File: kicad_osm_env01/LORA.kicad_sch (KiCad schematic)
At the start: 16 parts, among them J9 Conn_01x06, U16 RAK3172

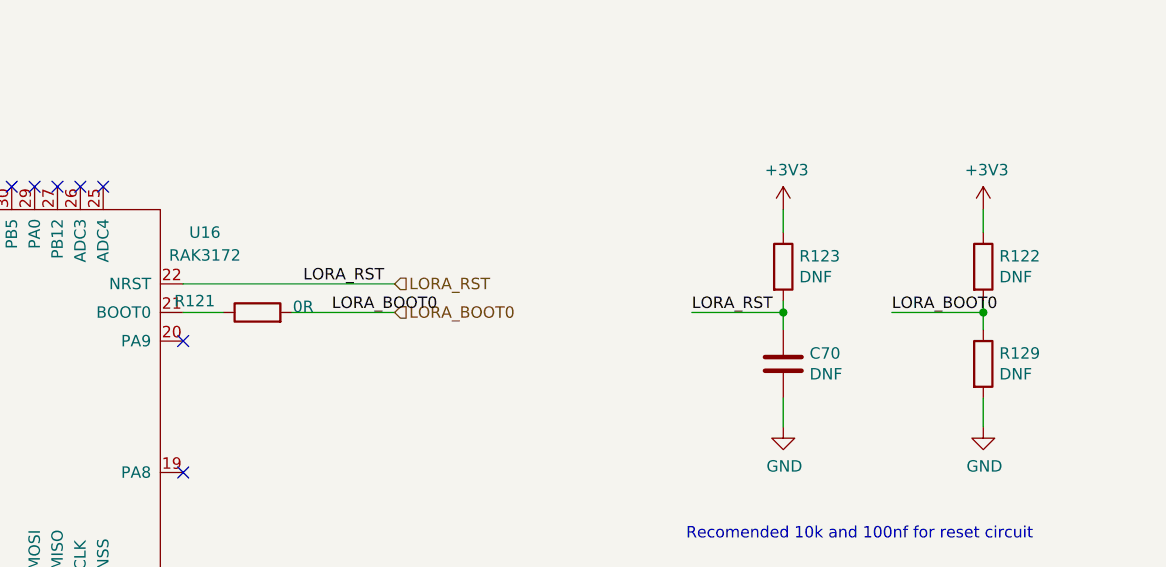
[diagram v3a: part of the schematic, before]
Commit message: updated schematics and added rs232
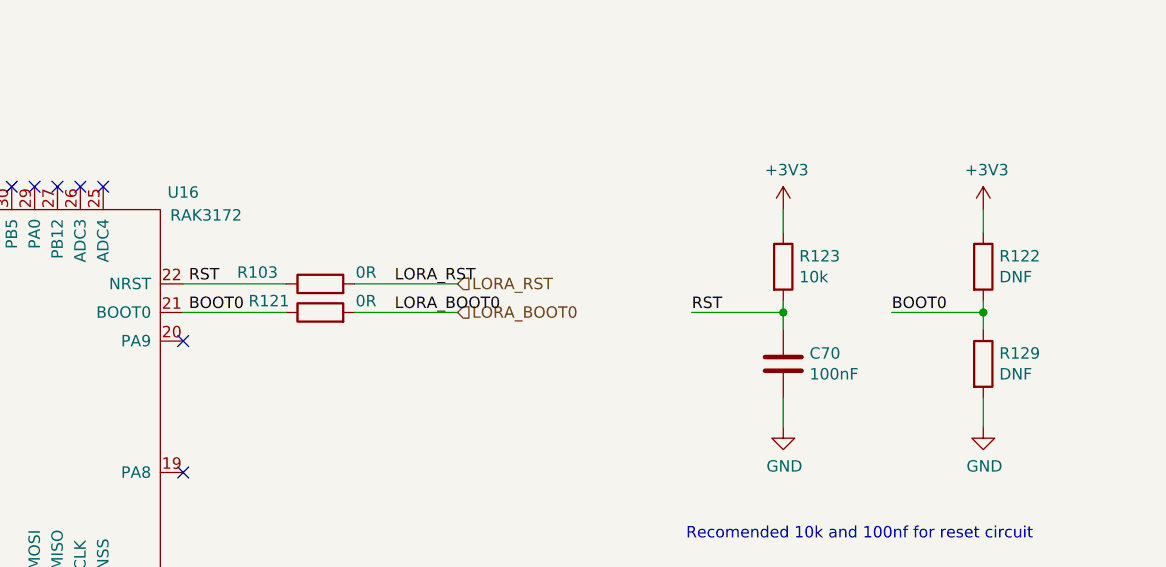
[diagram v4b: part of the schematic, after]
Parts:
- added R103: 0R, symbol device:R
- C70: value DNF -> 100nF
- R123: value DNF -> 10k
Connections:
- net LORA_BOOT0: no longer R122.2, R129.1
- net LORA_RST: now also R103.2; no longer C70.1, R123.2, U16.22 (NRST)
- net BOOT0: now reaches R121.1, U16.21 (BOOT0)
- net BOOT0: now also R122.2, R129.1
- new net RST: C70.1, R103.1, R123.2, U16.22 (NRST)
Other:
- moved on the sheet: R121
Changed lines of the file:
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@@
     (stroke (width 0) (type default) (color 0 0 0 0))
   )
-  (wire (pts (xy 181.61 72.39) (xy 193.04 72.39))
+  (wire (pts (xy 188.595 72.39) (xy 200.025 72.39))
     (stroke (width 0) (type default) (color 0 0 0 0))
   )
@@
     (stroke (width 0) (type default) (color 0 0 0 0))
   )
+  (wire (pts (xy 188.595 69.215) (xy 200.025 69.215))
+    (stroke (width 0) (type default) (color 0 0 0 0))
+  )
   (wire (pts (xy 132.08 110.49) (xy 132.08 109.22))
     (stroke (width 0) (type default) (color 0 0 0 0))
@@
     (stroke (width 0) (type default) (color 0 0 0 0))
   )
-  (wire (pts (xy 169.545 69.215) (xy 193.04 69.215))
-    (stroke (width 0) (type default) (color 0 0 0 0))
-  )
-  (wire (pts (xy 169.545 72.39) (xy 173.99 72.39))
+  (wire (pts (xy 169.545 72.39) (xy 180.975 72.39))
     (stroke (width 0) (type default) (color 0 0 0 0))
   )
@@
   )
   (wire (pts (xy 104.14 71.755) (xy 91.44 71.755))
+    (stroke (width 0) (type default) (color 0 0 0 0))
+  )
+  (wire (pts (xy 169.545 69.215) (xy 180.975 69.215))
     (stroke (width 0) (type default) (color 0 0 0 0))
   )
@@
     (effects (font (size 1.27 1.27)) (justify right bottom))
   )
-  (label "LORA_RST" (at 226.06 72.39 0)
+  (label "RST" (at 226.06 72.39 0)
     (effects (font (size 1.27 1.27)) (justify left bottom))
   )
@@
     (effects (font (size 1.27 1.27)) (justify right bottom))
   )
-  (label "LORA_RST" (at 182.88 69.215 0)
-    (effects (font (size 1.27 1.27)) (justify left bottom))
-  )
-  (label "LORA_BOOT0" (at 186.055 72.39 0)
-    (effects (font (size 1.27 1.27)) (justify left bottom))
-  )
-  (label "LORA_BOOT0" (at 248.285 72.39 0)
+  (label "LORA_RST" (at 193.04 69.215 0)
+    (effects (font (size 1.27 1.27)) (justify left bottom))
+  )
+  (label "LORA_BOOT0" (at 193.04 72.39 0)
+    (effects (font (size 1.27 1.27)) (justify left bottom))
+  )
+  (label "BOOT0" (at 248.285 72.39 0)
     (effects (font (size 1.27 1.27)) (justify left bottom))
   )
@@
     (effects (font (size 1.27 1.27)) (justify right bottom))
   )
+  (label "BOOT0" (at 170.18 72.39 0)
+    (effects (font (size 1.27 1.27)) (justify left bottom))
+  )
   (label "LORA_RST" (at 50.8 173.99 180)
     (effects (font (size 1.27 1.27)) (justify right bottom))
   )
-  (hierarchical_label "LORA_RST" (shape input) (at 193.04 69.215 0)
+  (label "RST" (at 170.18 69.215 0)
+    (effects (font (size 1.27 1.27)) (justify left bottom))
+  )
+  (hierarchical_label "LORA_RST" (shape input) (at 200.025 69.215 0)
     (effects (font (size 1.27 1.27)) (justify left))
   )
@@
     (effects (font (size 1.27 1.27)) (justify right))
   )
-  (hierarchical_label "LORA_BOOT0" (shape input) (at 193.04 72.39 0)
+  (hierarchical_label "LORA_BOOT0" (shape input) (at 200.025 72.39 0)
     (effects (font (size 1.27 1.27)) (justify left))
   )
@@
       (effects (font (size 1.27 1.27)) (justify left))
     )
-    (property "Value" "DNF" (id 1) (at 237.998 68.453 0)
+    (property "Value" "10k" (id 1) (at 237.998 68.453 0)
       (effects (font (size 1.27 1.27)) (justify left))
     )
@@
       (effects (font (size 1.27 1.27)) (justify left))
     )
-    (property "Value" "DNF" (id 1) (at 239.141 79.248 0)
+    (property "Value" "100nF" (id 1) (at 239.141 79.248 0)
       (effects (font (size 1.27 1.27)) (justify left))
     )
@@
     (pin "2")
   )
+  (symbol (lib_id "device:R") (at 184.785 69.215 90) (unit 1)
+    (in_bom yes) (on_board yes)
+    (property "Reference" "R103" (id 0) (at 177.8 67.945 90))
+    (property "Value" "0R" (id 1) (at 189.865 67.945 90))
+    (property "Footprint" "" (id 2) (at 184.785 70.993 90)
+      (effects (font (size 1.27 1.27)) hide)
+    )
+    (property "Datasheet" "" (id 3) (at 184.785 69.215 0)
+      (effects (font (size 1.27 1.27)) hide)
+    )
+    (pin "1")
+    (pin "2")
+  )
   (symbol (lib_id "device:Jumper_NO_Small") (at 117.475 81.28 0) (unit 1)
     (in_bom yes) (on_board yes) (fields_autoplaced)
@@
   )
   (symbol (lib_id "Devtank:RAK3172") (at 147.32 83.185 0) (unit 1)
-    (in_bom yes) (on_board yes) (fields_autoplaced)
-    (property "Reference" "U16" (id 0) (at 171.9527 63.5085 0))
-    (property "Value" "RAK3172" (id 1) (at 171.9527 66.0454 0))
+    (in_bom yes) (on_board yes)
+    (property "Reference" "U16" (id 0) (at 169.545 59.055 0))
+    (property "Value" "RAK3172" (id 1) (at 172.085 61.595 0))
     (property "Footprint" "" (id 2) (at 140.97 71.755 0)
       (effects (font (size 1.27 1.27)) hide)
@@
     (pin "6")
   )
-  (symbol (lib_id "device:R") (at 177.8 72.39 90) (unit 1)
-    (in_bom yes) (on_board yes)
-    (property "Reference" "R121" (id 0) (at 170.815 71.12 90))
-    (property "Value" "0R" (id 1) (at 182.88 71.755 90))
-    (property "Footprint" "" (id 2) (at 177.8 74.168 90)
-      (effects (font (size 1.27 1.27)) hide)
-    )
-    (property "Datasheet" "" (id 3) (at 177.8 72.39 0)
-      (effects (font (size 1.27 1.27)) hide)
-    )
+  (symbol (lib_id "device:R") (at 184.785 72.39 90) (unit 1)
+    (in_bom yes) (on_board yes)
+    (property "Reference" "R121" (id 0) (at 179.07 71.12 90))
+    (property "Value" "0R" (id 1) (at 189.865 71.12 90))
+    (property "Footprint" "" (id 2) (at 184.785 74.168 90)
+      (effects (font (size 1.27 1.27)) hide)
+    )
+    (property "Datasheet" "" (id 3) (at 184.785 72.39 0)
+      (effects (font (size 1.27 1.27)) hide)
+    )

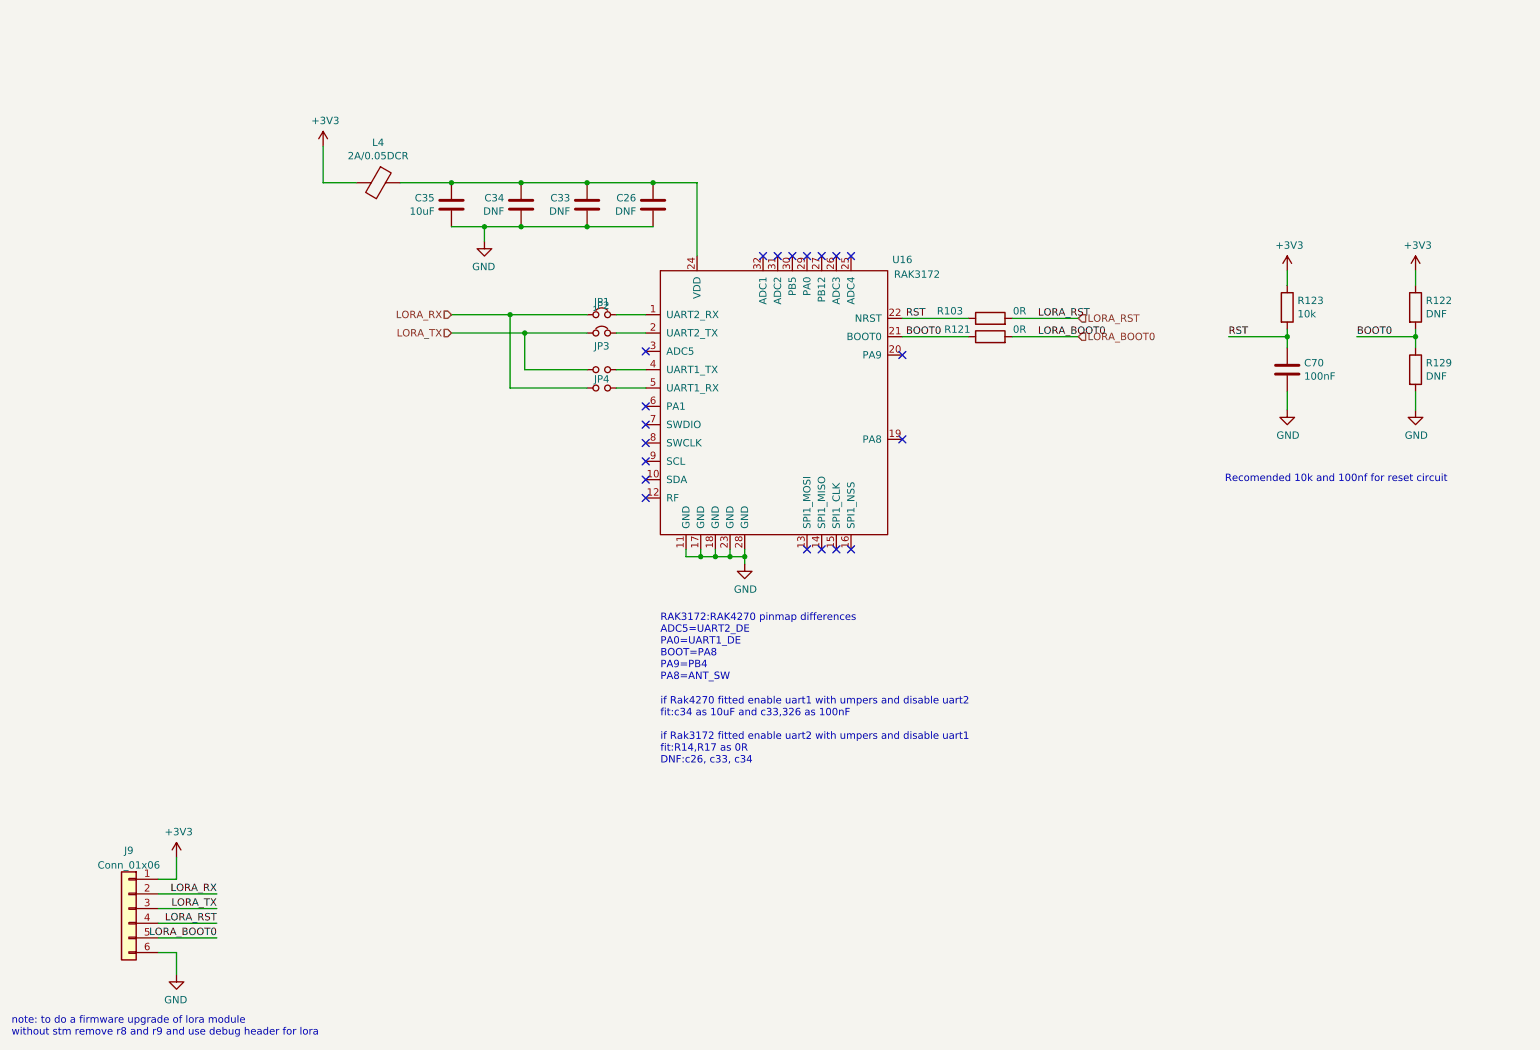
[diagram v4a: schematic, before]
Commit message: Schematics waiting review
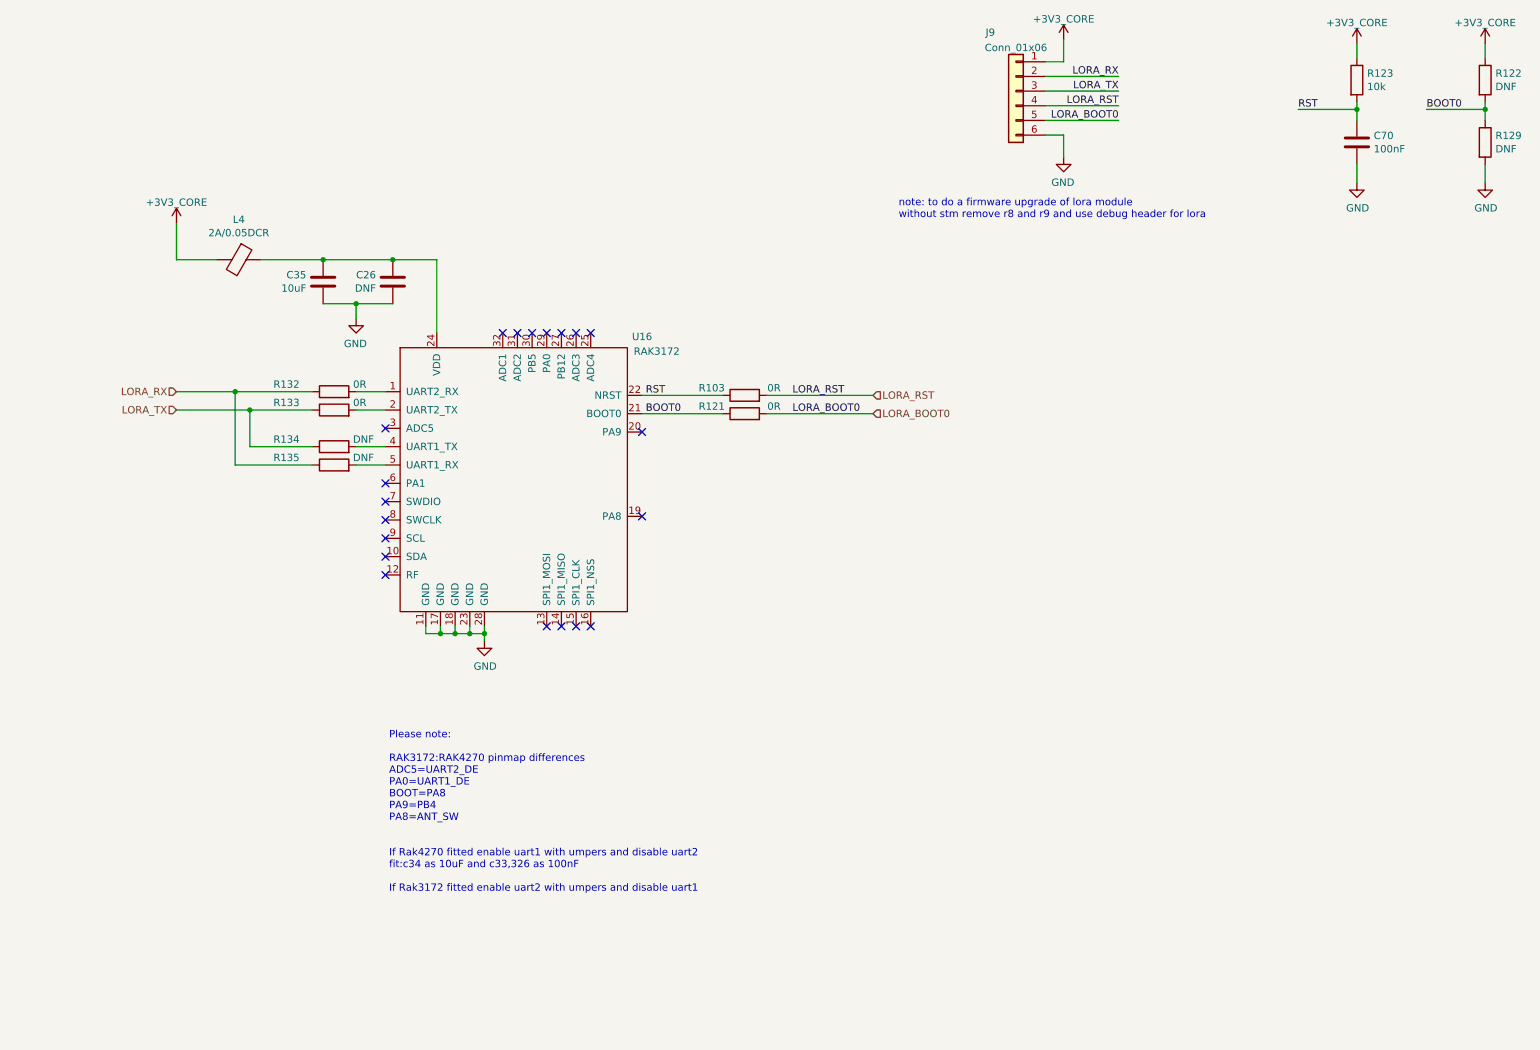
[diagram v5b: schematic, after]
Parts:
- removed C33: DNF, Capacitor_SMD:C_0402_1005Metric, symbol device:C
- removed C34: DNF, Capacitor_SMD:C_0603_1608Metric, symbol device:C
- removed JP1: Jumper_NC_Small, symbol device:Jumper_NC_Small
- removed JP2: ~, symbol device:Jumper_NC_Small
- removed JP3: ~, symbol device:Jumper_NO_Small
- removed JP4: Jumper_NO_Small, symbol device:Jumper_NO_Small
- added R132, R133: 0R, symbol device:R
- added R134, R135: DNF, symbol device:R
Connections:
- net LORA_RX: now also R132.1, R135.1
- net LORA_TX: now also R133.1, R134.1
- net at U16.4 (UART1_TX): now also R134.2
- net at U16.5 (UART1_RX): now also R135.2
- net at U16.1 (UART2_RX): now also R132.2
- net at U16.2 (UART2_TX): now also R133.2
- net +3V3 renamed +3V3_CORE
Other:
- note added: "Please note: RAK3172:RAK4270 pinmap differences ADC5=UART2_DE PA0=UART1_DE BOOT=PA8 PA9=PB4 PA8=ANT_SW If Rak4270 fitted enable uart1 with umpers and disable uart2 fit:c34 as 10uF and c33,326 as 100nF If Rak3172 fitted enable uart2 with umpers and disable uart1"
- note removed: "RAK3172:RAK4270 pinmap differences ADC5=UART2_DE PA0=UART1_DE BOOT=PA8 PA9=PB4 PA8=ANT_SW"
- note removed: "Recomended 10k and 100nf for reset circuit"
- note removed: "if Rak4270 fitted enable uart1 with umpers and disable uart2 fit:c34 as 10uF and c33,326 as 100nF if Rak3172 fitted enable uart2 with umpers and disable uart1 fit:R14,R17 as 0R DNF:c26, c33, c34"
- moved on the sheet: C26, C35, C70, J9, L4, R103, R121, R122, R123, R129, U16

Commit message: before fixing devtank symbol issues
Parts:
- J9: value Conn_01x06 -> (none); symbol Connector:Conn_01x06 -> Connector_Generic:Conn_01x06
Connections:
- net BOOT0 is gone; now on net LORA_BOOT0: R121.1, R122.2, R129.1, U16.21 (BOOT0)
- net LORA_RST: no longer J9.4 (Pin_4)
- net RST renamed LORA_NRST
- net LORA_NRST: now also J9.4 (Pin_4)
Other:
- note added: "note: to do a firmware upgrade of lora module without stm remove r132 and r133 and use debug header for lora"
- note removed: "note: to do a firmware upgrade of lora module without stm remove r8 and r9 and use debug header for lora"
- moved on the sheet: R103, R121
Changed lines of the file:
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@@
     (stroke (width 0) (type default) (color 0 0 0 0))
   )
-  (wire (pts (xy 146.05 85.725) (xy 164.465 85.725))
+  (wire (pts (xy 151.13 85.725) (xy 164.465 85.725))
     (stroke (width 0) (type default) (color 0 0 0 0))
   )
@@
     (stroke (width 0) (type default) (color 0 0 0 0))
   )
-  (wire (pts (xy 146.05 82.55) (xy 164.465 82.55))
+  (wire (pts (xy 151.13 82.55) (xy 164.465 82.55))
     (stroke (width 0) (type default) (color 0 0 0 0))
   )
@@
     (stroke (width 0) (type default) (color 0 0 0 0))
   )
-  (wire (pts (xy 238.125 33.02) (xy 248.285 33.02))
+  (wire (pts (xy 236.855 33.02) (xy 248.285 33.02))
     (stroke (width 0) (type default) (color 0 0 0 0))
   )
@@
     (stroke (width 0) (type default) (color 0 0 0 0))
   )
-  (wire (pts (xy 124.46 85.725) (xy 138.43 85.725))
+  (wire (pts (xy 124.46 85.725) (xy 143.51 85.725))
     (stroke (width 0) (type default) (color 0 0 0 0))
   )
@@
     (stroke (width 0) (type default) (color 0 0 0 0))
   )
-  (wire (pts (xy 260.35 33.02) (xy 270.51 33.02))
+  (wire (pts (xy 257.81 33.02) (xy 270.51 33.02))
     (stroke (width 0) (type default) (color 0 0 0 0))
   )
@@
     (stroke (width 0) (type default) (color 0 0 0 0))
   )
-  (wire (pts (xy 124.46 82.55) (xy 138.43 82.55))
-    (stroke (width 0) (type default) (color 0 0 0 0))
-  )
-  (text "note: to do a firmware upgrade of lora module\nwithout stm remove r8 and r9 and use debug header for lora"
+  (wire (pts (xy 124.46 82.55) (xy 143.51 82.55))
+    (stroke (width 0) (type default) (color 0 0 0 0))
+  )
+  (text "note: to do a firmware upgrade of lora module\nwithout stm remove r132 and r133 and use debug header for lora"
     (at 168.91 52.07 0)
     (effects (font (size 1.27 1.27)) (justify left bottom))
@@
     (effects (font (size 1.27 1.27)) (justify right bottom))
   )
-  (label "RST" (at 238.125 33.02 0)
-    (effects (font (size 1.27 1.27)) (justify left bottom))
-  )
   (label "LORA_RX" (at 207.01 27.305 180)
     (effects (font (size 1.27 1.27)) (justify right bottom))
   )
-  (label "LORA_RST" (at 150.495 82.55 0)
-    (effects (font (size 1.27 1.27)) (justify left bottom))
-  )
-  (label "LORA_BOOT0" (at 150.495 85.725 0)
-    (effects (font (size 1.27 1.27)) (justify left bottom))
-  )
-  (label "BOOT0" (at 260.35 33.02 0)
+  (label "LORA_BOOT0" (at 257.81 33.02 0)
     (effects (font (size 1.27 1.27)) (justify left bottom))
   )
@@
     (effects (font (size 1.27 1.27)) (justify right bottom))
   )
-  (label "BOOT0" (at 125.095 85.725 0)
+  (label "LORA_BOOT0" (at 125.095 85.725 0)
     (effects (font (size 1.27 1.27)) (justify left bottom))
   )
-  (label "LORA_RST" (at 207.01 32.385 180)
+  (label "LORA_NRST" (at 236.855 33.02 0)
+    (effects (font (size 1.27 1.27)) (justify left bottom))
+  )
+  (label "LORA_NRST" (at 207.01 32.385 180)
     (effects (font (size 1.27 1.27)) (justify right bottom))
   )
-  (label "RST" (at 125.095 82.55 0)
+  (label "LORA_NRST" (at 125.095 82.55 0)
     (effects (font (size 1.27 1.27)) (justify left bottom))
   )
@@
     (pin "1")
   )
-  (symbol (lib_id "device:R") (at 142.24 82.55 90) (unit 1)
-    (in_bom yes) (on_board yes)
-    (property "Reference" "R103" (id 0) (at 136.525 81.28 90))
-    (property "Value" "0R" (id 1) (at 147.32 81.28 90))
-    (property "Footprint" "" (id 2) (at 142.24 84.328 90)
-      (effects (font (size 1.27 1.27)) hide)
-    )
-    (property "Datasheet" "" (id 3) (at 142.24 82.55 0)
+  (symbol (lib_id "device:R") (at 147.32 82.55 90) (unit 1)
+    (in_bom yes) (on_board yes)
+    (property "Reference" "R103" (id 0) (at 141.605 81.28 90))
+    (property "Value" "0R" (id 1) (at 152.4 81.28 90))
+    (property "Footprint" "" (id 2) (at 147.32 84.328 90)
+      (effects (font (size 1.27 1.27)) hide)
+    )
+    (property "Datasheet" "" (id 3) (at 147.32 82.55 0)
       (effects (font (size 1.27 1.27)) hide)
     )
@@
     (pin "1")
   )
-  (symbol (lib_id "Connector:Conn_01x06") (at 189.23 29.845 0) (mirror y) (unit 1)
+  (symbol (lib_id "Connector_Generic:Conn_01x06") (at 189.23 29.845 0) (mirror y) (unit 1)
     (in_bom yes) (on_board yes)
     (property "Reference" "J9" (id 0) (at 184.785 19.685 0))
-    (property "Value" "Conn_01x06" (id 1) (at 189.23 22.3321 0))
+    (property "Value" "" (id 1) (at 189.23 22.3321 0))
     (property "Footprint" "" (id 2) (at 189.23 29.845 0)
       (effects (font (size 1.27 1.27)) hide)
@@
     (pin "2")
   )
-  (symbol (lib_id "device:R") (at 142.24 85.725 90) (unit 1)
-    (in_bom yes) (on_board yes)
-    (property "Reference" "R121" (id 0) (at 136.525 84.455 90))
-    (property "Value" "0R" (id 1) (at 147.32 84.455 90))
-    (property "Footprint" "" (id 2) (at 142.24 87.503 90)
-      (effects (font (size 1.27 1.27)) hide)
-    )
-    (property "Datasheet" "" (id 3) (at 142.24 85.725 0)
-      (effects (font (size 1.27 1.27)) hide)
-    )
+  (symbol (lib_id "device:R") (at 147.32 85.725 90) (unit 1)
+    (in_bom yes) (on_board yes)
+    (property "Reference" "R121" (id 0) (at 141.605 84.455 90))
+    (property "Value" "0R" (id 1) (at 152.4 84.455 90))
+    (property "Footprint" "" (id 2) (at 147.32 87.503 90)
+      (effects (font (size 1.27 1.27)) hide)
+    )
+    (property "Datasheet" "" (id 3) (at 147.32 85.725 0)
+      (effects (font (size 1.27 1.27)) hide)
+    )
